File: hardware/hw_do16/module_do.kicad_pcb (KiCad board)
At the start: 2 copper layers, 89.5 x 62.2 mm, 132 parts, among them J1 DO_0, J2 DO_1, J3 MOD, P3 DEBUG, Q1 IRLML5103, Q10 IRLML5103, Q11 IRLML5103, Q12 IRLML5103, Q13 IRLML5103, Q14 IRLML5103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

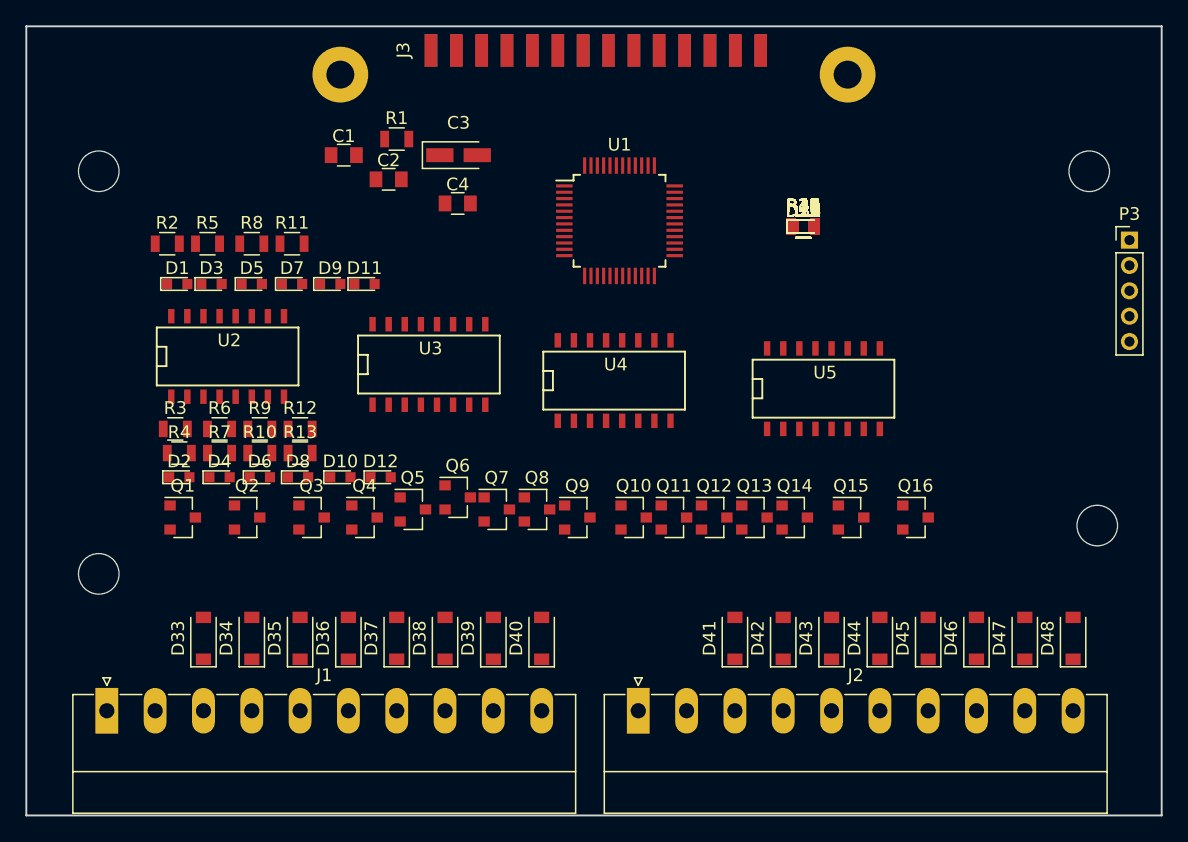
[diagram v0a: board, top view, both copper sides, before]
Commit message: Обновлена плата модуля DO16.
Завершена предварительная трассировка.
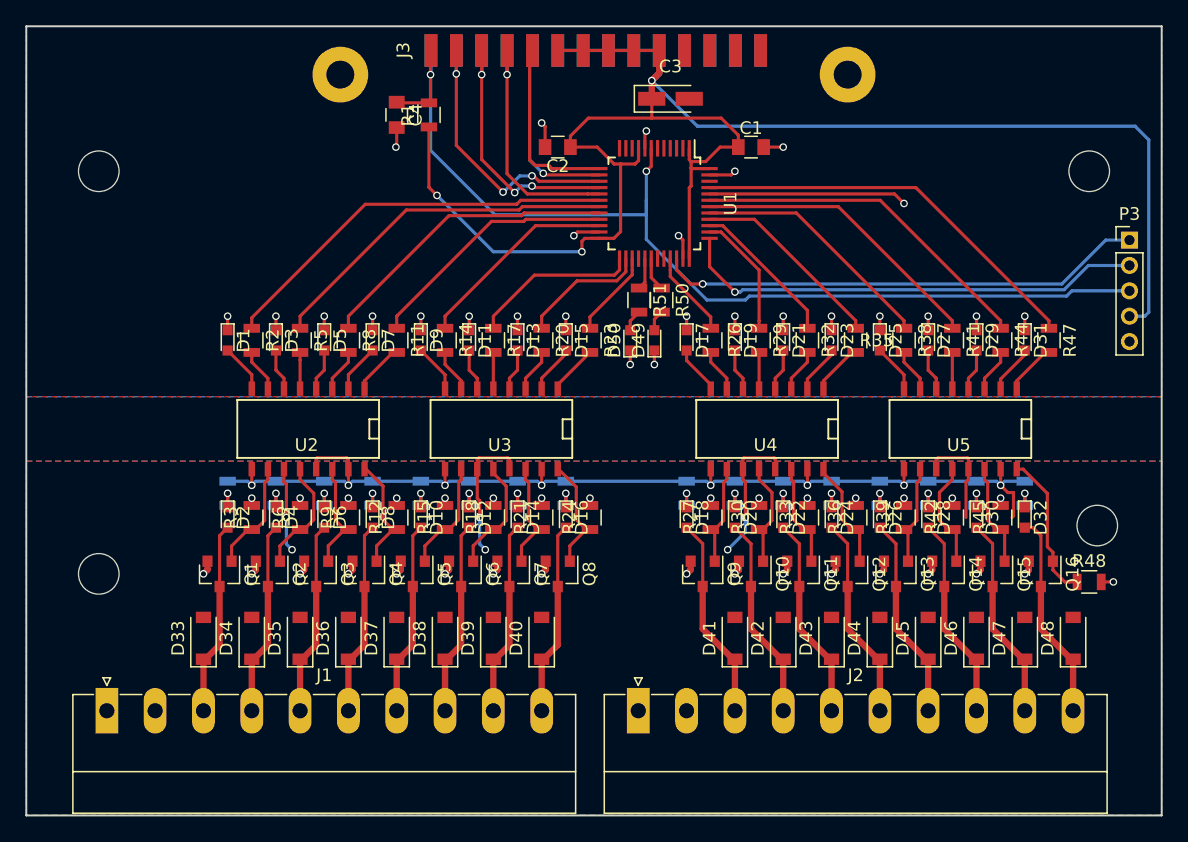
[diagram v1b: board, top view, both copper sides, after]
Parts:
- added D49: SOK, LEDs:LED_0603, F.Cu at (149.2, 87.6)
- added D50: SFL, LEDs:LED_0603, F.Cu at (147.3, 87.6)
- added R50: 1k, Resistors_SMD:R_0805, F.Cu at (149.8, 84.5)
- added R51: 1k, Resistors_SMD:R_0805, F.Cu at (148.0, 84.5)
- R10, R13, R16, R19, R22, R25, R28, R31, R34, R37, R4, R40, R43, R46, R49, R7: moved to B.Cu
- moved R16 36.8 mm to (130.8, 99.7), turned to 90 degrees
- moved R15 36.4 mm to (132.7, 101.6), turned to 90 degrees
- moved R48 36.0 mm to (183.5, 106.7)
- moved R19 33.7 mm to (134.6, 99.7), turned to 90 degrees
- moved R18 33.5 mm to (136.5, 101.6), turned to 90 degrees
- moved D14 32.2 mm to (138.4, 101.6), turned to 270 degrees
- moved C1 32.1 mm to (156.8, 72.4)
- moved R21 30.9 mm to (140.3, 101.6), turned to 90 degrees
- moved R22 30.8 mm to (138.4, 99.7), turned to 90 degrees
- moved R14 29.6 mm to (132.7, 87.6), turned to 270 degrees
- moved D16 29.6 mm to (142.2, 101.6), turned to 270 degrees
- moved D32 28.8 mm to (178.4, 101.6), turned to 270 degrees
- moved R24 28.5 mm to (144.1, 101.6), turned to 90 degrees
- moved R25 28.2 mm to (142.2, 99.7), turned to 90 degrees
- moved R45 27.7 mm to (176.5, 101.6), turned to 90 degrees
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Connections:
- U1 pad 10: DO0 -> Net-(U1-Pad10)
- U1 pad 11: DO1 -> Net-(U1-Pad11)
- U1 pad 18: DO2 -> DO0
- U1 pad 19: DO3 -> DO1
- U1 pad 20: DO4 -> DO2
- U1 pad 21: DO5 -> DO3
- U1 pad 22: DO6 -> DO4
- U1 pad 25: DO7 -> DO5
- U1 pad 26: Net-(U1-Pad26) -> DO6
- U1 pad 27: Net-(U1-Pad27) -> DO7
- U1 pad 29: Net-(U1-Pad29) -> SFL
- U1 pad 30: Net-(U1-Pad30) -> SOK
- U1 pad 33: Net-(U1-Pad33) -> DO8
- U1 pad 38: DO8 -> DO9
- U1 pad 39: DO9 -> DO10
- U1 pad 40: DO10 -> DO11
- U1 pad 41: DO11 -> DO12
- U1 pad 42: DO12 -> DO13
- U1 pad 43: DO13 -> DO14
- U1 pad 45: DO14 -> DO15
- U1 pad 46: DO15 -> Net-(U1-Pad46)
- U2 pad 1: Net-(R2-Pad2) -> Net-(R11-Pad2)
- U2 pad 10: Net-(Q4-Pad1) -> Net-(Q1-Pad1)
- U2 pad 12: Net-(Q3-Pad1) -> Net-(Q2-Pad1)
- U2 pad 14: Net-(Q2-Pad1) -> Net-(Q3-Pad1)
- U2 pad 16: Net-(Q1-Pad1) -> Net-(Q4-Pad1)
- U2 pad 2: Net-(D1-Pad2) -> Net-(D7-Pad2)
- U2 pad 3: Net-(R5-Pad2) -> Net-(R8-Pad2)
- U2 pad 4: Net-(D3-Pad2) -> Net-(D5-Pad2)
- U2 pad 5: Net-(R8-Pad2) -> Net-(R5-Pad2)
- U2 pad 6: Net-(D5-Pad2) -> Net-(D3-Pad2)
- U2 pad 7: Net-(R11-Pad2) -> Net-(R2-Pad2)
- U2 pad 8: Net-(D7-Pad2) -> Net-(D1-Pad2)
- U3 pad 1: Net-(R14-Pad2) -> Net-(R23-Pad2)
- U3 pad 10: Net-(Q8-Pad1) -> Net-(Q5-Pad1)
- U3 pad 12: Net-(Q7-Pad1) -> Net-(Q6-Pad1)
- U3 pad 14: Net-(Q6-Pad1) -> Net-(Q7-Pad1)
- U3 pad 16: Net-(Q5-Pad1) -> Net-(Q8-Pad1)
- U3 pad 2: Net-(D9-Pad2) -> Net-(D15-Pad2)
- U3 pad 3: Net-(R17-Pad2) -> Net-(R20-Pad2)
- U3 pad 4: Net-(D11-Pad2) -> Net-(D13-Pad2)
- U3 pad 5: Net-(R20-Pad2) -> Net-(R17-Pad2)
- U3 pad 6: Net-(D13-Pad2) -> Net-(D11-Pad2)
- U3 pad 7: Net-(R23-Pad2) -> Net-(R14-Pad2)
- U3 pad 8: Net-(D15-Pad2) -> Net-(D9-Pad2)
- U4 pad 1: Net-(R26-Pad2) -> Net-(R35-Pad2)
- U4 pad 10: Net-(Q12-Pad1) -> Net-(Q9-Pad1)
- U4 pad 12: Net-(Q11-Pad1) -> Net-(Q10-Pad1)
- U4 pad 14: Net-(Q10-Pad1) -> Net-(Q11-Pad1)
- U4 pad 16: Net-(Q9-Pad1) -> Net-(Q12-Pad1)
- U4 pad 2: Net-(D17-Pad2) -> Net-(D23-Pad2)
- U4 pad 3: Net-(R29-Pad2) -> Net-(R32-Pad2)
- U4 pad 4: Net-(D19-Pad2) -> Net-(D21-Pad2)
- U4 pad 5: Net-(R32-Pad2) -> Net-(R29-Pad2)
- U4 pad 6: Net-(D21-Pad2) -> Net-(D19-Pad2)
- U4 pad 7: Net-(R35-Pad2) -> Net-(R26-Pad2)
- U4 pad 8: Net-(D23-Pad2) -> Net-(D17-Pad2)
- U5 pad 1: Net-(R38-Pad2) -> Net-(R47-Pad2)
- U5 pad 10: Net-(Q16-Pad1) -> Net-(Q13-Pad1)
- U5 pad 12: Net-(Q15-Pad1) -> Net-(Q14-Pad1)
- U5 pad 14: Net-(Q14-Pad1) -> Net-(Q15-Pad1)
- U5 pad 16: Net-(Q13-Pad1) -> Net-(Q16-Pad1)
- U5 pad 2: Net-(D25-Pad2) -> Net-(D31-Pad2)
- U5 pad 3: Net-(R41-Pad2) -> Net-(R44-Pad2)
- U5 pad 4: Net-(D27-Pad2) -> Net-(D29-Pad2)
- U5 pad 5: Net-(R44-Pad2) -> Net-(R41-Pad2)
- U5 pad 6: Net-(D29-Pad2) -> Net-(D27-Pad2)
- U5 pad 7: Net-(R47-Pad2) -> Net-(R38-Pad2)
- U5 pad 8: Net-(D31-Pad2) -> Net-(D25-Pad2)
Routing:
- net VDD: track 0.00 -> 146.7 mm, vias 0 -> 3
- net DO0v: track 0.00 -> 119.4 mm, vias 0 -> 14
- net RESET: track 0.00 -> 82.6 mm, vias 0 -> 2
- net VSS: track 0.00 -> 48.3 mm, vias 0 -> 26
- net SWDIO: track 0.00 -> 38.5 mm, vias 0 -> 1
- net SWCLK: track 0.00 -> 37.0 mm, vias 0 -> 1
- net DO0: track 0.00 -> 32.1 mm
- net DO15: track 0.00 -> 31.7 mm
- net DO1: track 0.00 -> 28.1 mm
- net DO24v: track 0.00 -> 27.7 mm, vias 0 -> 32
- net DO14: track 0.00 -> 27.5 mm
- net DO2: track 0.00 -> 24.1 mm
- net DO13: track 0.00 -> 23.5 mm
- net SPI_SCK: track 0.00 -> 22.8 mm, vias 0 -> 3
- net SPI_MISO: track 0.00 -> 21.1 mm, vias 0 -> 3
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- added copper zone on F.Cu, net DO0v
- added copper zone on B.Cu, net DO24v
- added copper zone on B.Cu, net VSS
- added copper zone on F.Cu, net VSS

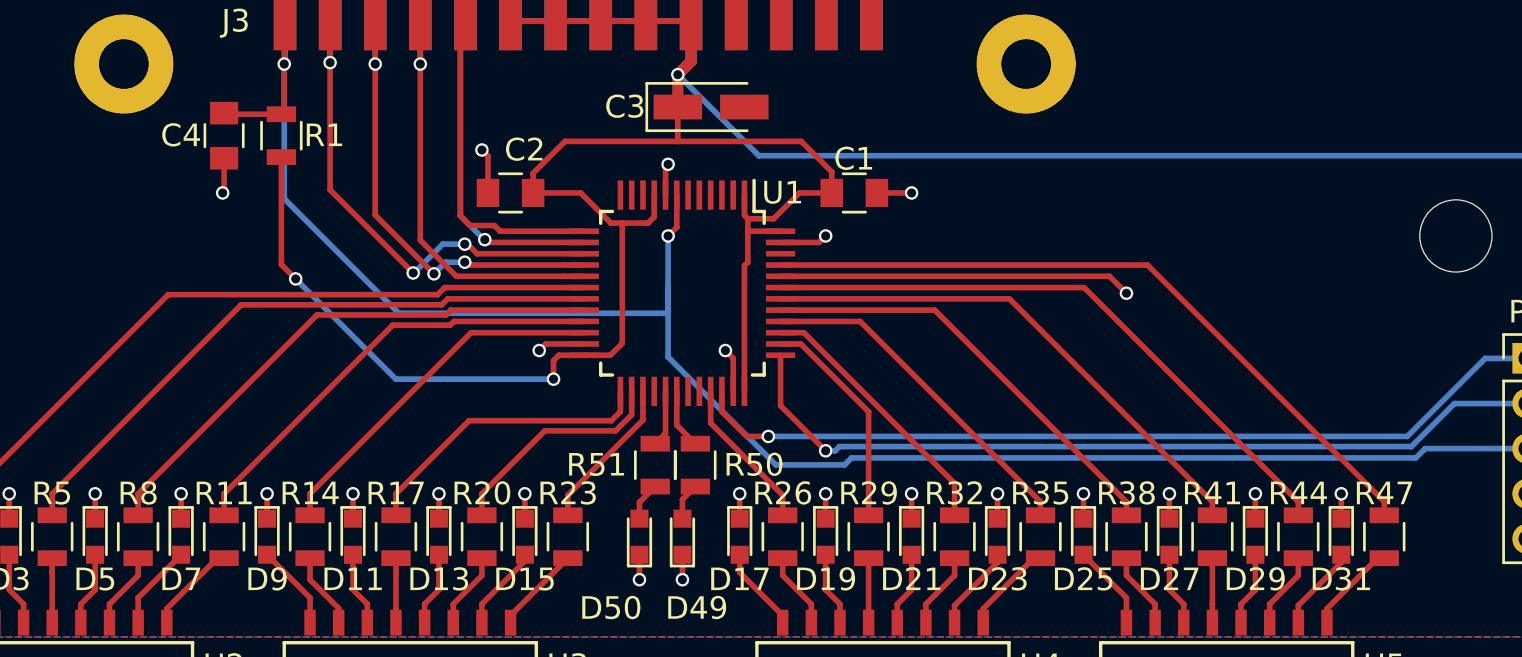
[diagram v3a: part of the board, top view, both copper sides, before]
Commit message: Обновлены платы модулей.
Добавлен разъем для работы с аппаратным загрузчиком.
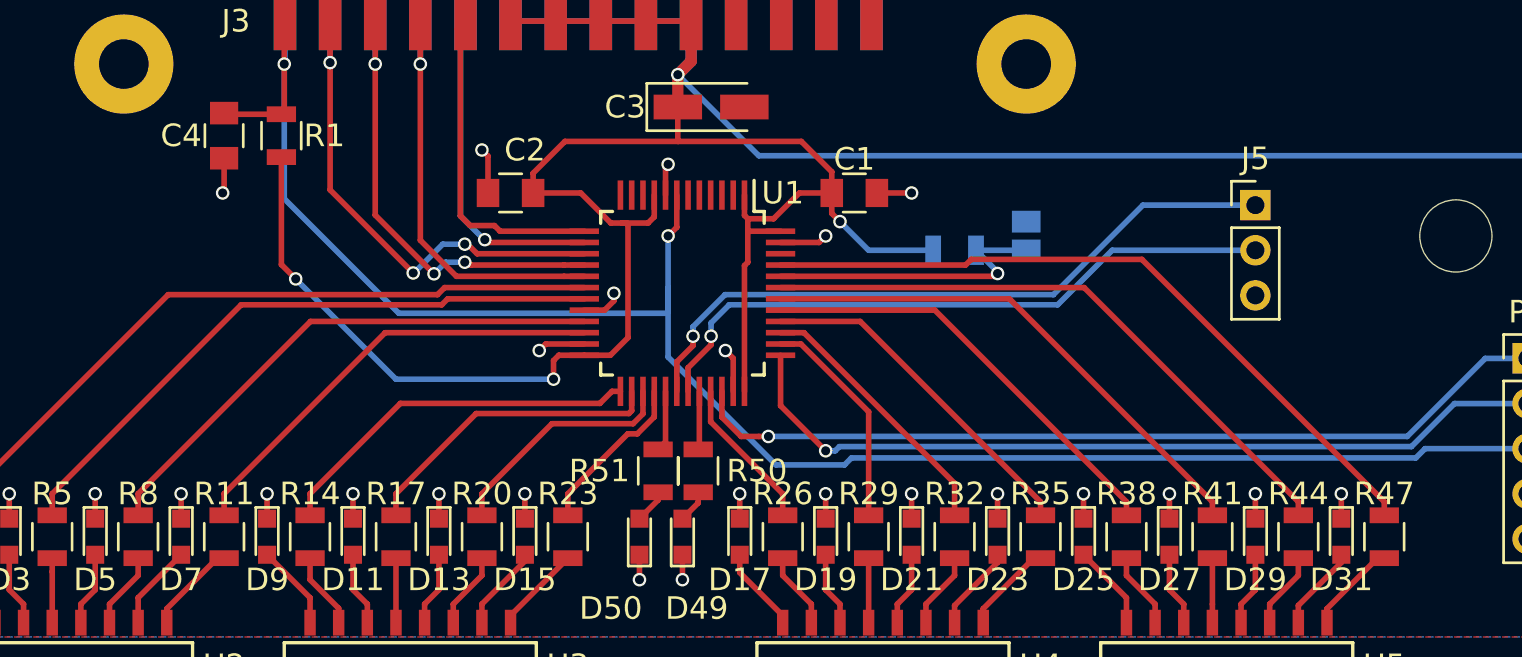
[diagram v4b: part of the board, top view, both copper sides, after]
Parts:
- added J4: BOOT0, Connect:GS2, B.Cu at (164.5, 74.3)
- added J5: UART1, Pin_Headers:Pin_Header_Straight_1x03_Pitch2.00mm, F.Cu at (174.6, 72.9)
- added R52: 10k, Resistors_SMD:R_0805, B.Cu at (161.3, 74.9)
- moved R51 0.28 mm to (148.1, 84.7)
- moved R50 0.28 mm to (149.9, 84.7)
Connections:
- C1 pad 2: VSS -> BOOT1
- C2 pad 2: VSS -> BOOT1
- C3 pad 2: VSS -> BOOT1
- C4 pad 2: VSS -> BOOT1
- D1 pad 1: VSS -> BOOT1
- D11 pad 1: VSS -> BOOT1
- D13 pad 1: VSS -> BOOT1
- D15 pad 1: VSS -> BOOT1
- D17 pad 1: VSS -> BOOT1
- D19 pad 1: VSS -> BOOT1
- D21 pad 1: VSS -> BOOT1
- D23 pad 1: VSS -> BOOT1
- D25 pad 1: VSS -> BOOT1
- D27 pad 1: VSS -> BOOT1
- D29 pad 1: VSS -> BOOT1
- D3 pad 1: VSS -> BOOT1
- D31 pad 1: VSS -> BOOT1
- D49 pad 1: VSS -> BOOT1
- D5 pad 1: VSS -> BOOT1
- D50 pad 1: VSS -> BOOT1
- D7 pad 1: VSS -> BOOT1
- D9 pad 1: VSS -> BOOT1
- J3 pad 21: VSS -> BOOT1
- J3 pad 22: VSS -> BOOT1
- J3 pad 23: VSS -> BOOT1
- J3 pad 24: VSS -> BOOT1
- J3 pad 25: VSS -> BOOT1
- J3 pad 26: VSS -> BOOT1
- J3 pad 27: VSS -> BOOT1
- J3 pad 28: VSS -> BOOT1
- P3 pad 5: VSS -> BOOT1
- U1 pad 20: DO2 -> BOOT1
- U1 pad 21: DO3 -> DO2
- U1 pad 22: DO4 -> DO3
- U1 pad 23: VSS -> BOOT1
- U1 pad 25: DO5 -> DO4
- U1 pad 26: DO6 -> DO5
- U1 pad 27: DO7 -> DO6
- U1 pad 28: Net-(U1-Pad28) -> DO7
- U1 pad 30: SOK -> TX
- U1 pad 31: Net-(U1-Pad31) -> RX
- U1 pad 32: Net-(U1-Pad32) -> SOK
- U1 pad 35: VSS -> BOOT1
- U1 pad 44: VSS -> BOOT0
- U1 pad 47: VSS -> BOOT1
- U1 pad 8: VSS -> BOOT1
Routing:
- net VSS: track 48.3 -> 0.00 mm, vias 26 -> 0
- net BOOT1: track 0.00 -> 34.4 mm, vias 0 -> 26
- net TX: track 0.00 -> 30.3 mm, vias 0 -> 1
- net RX: track 0.00 -> 28.9 mm, vias 0 -> 1
- net BOOT0: track 0.00 -> 13.3 mm, vias 0 -> 1
- net VDD: track 146.7 -> 153.1 mm, vias 3 -> 4
- net DO4: track 16.1 -> 16.6 mm
- added copper zone on B.Cu, net BOOT1
- added copper zone on F.Cu, net BOOT1
- removed copper zone on B.Cu, net VSS
- removed copper zone on F.Cu, net VSS
